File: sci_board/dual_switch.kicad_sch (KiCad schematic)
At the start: 5 parts, among them U8 MIC2009YM6-TR, U9 MIC2009YM6-TR

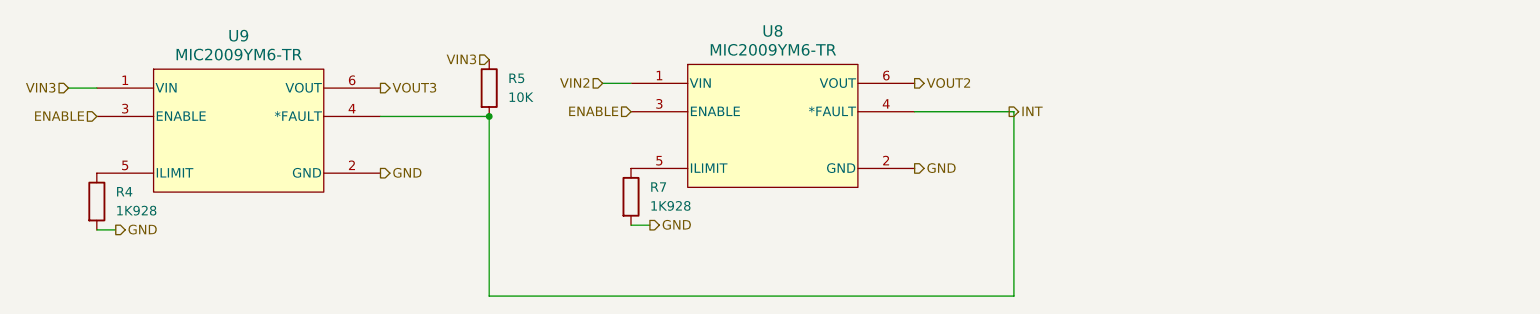
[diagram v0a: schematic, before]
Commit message: SCI board: add flash and mram; decorate PMC with boot, reset, etc
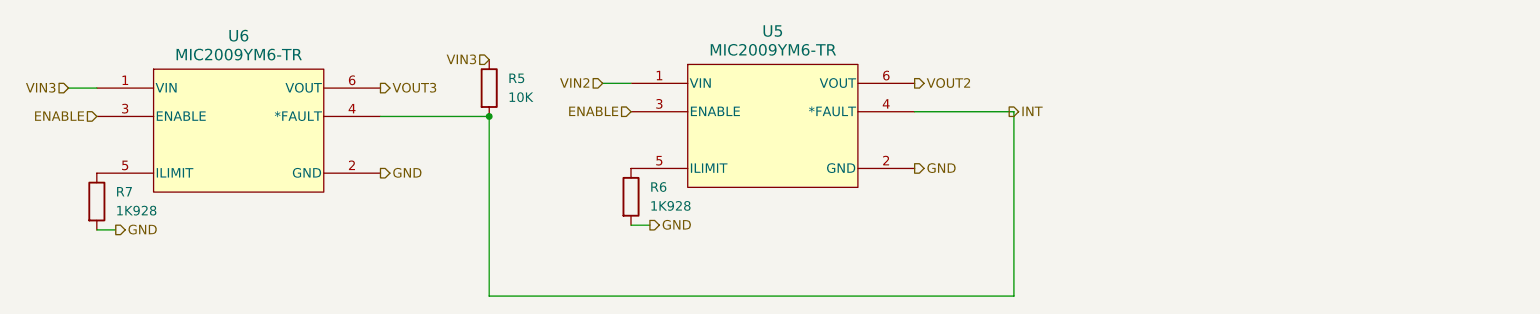
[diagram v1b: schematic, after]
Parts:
- renumbered R7 to R6, R4 to R7, U8 to U5, U9 to U6
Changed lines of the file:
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@@
 		(dnp no)
 		(fields_autoplaced yes)
-		(property "Reference" "U9"
+		(property "Reference" "U6"
 			(at 78.105 61.595 0)
 			(effects
@@
 		(instances
 			(project "sci_board"
-				(path "/b4b2c88d-f6cd-4e60-862d-e21f68728580/14f04065-33ea-4d2f-ac16-5b1240c79b45"
-					(reference "U11")
-					(unit 1)
-				)
-				(path "/b4b2c88d-f6cd-4e60-862d-e21f68728580/599e99f9-ecbe-4b40-92b0-d52ebb90431d"
-					(reference "U9")
-					(unit 1)
-				)
-				(path "/b4b2c88d-f6cd-4e60-862d-e21f68728580/9ec3d894-dc78-4c30-8f58-889c840122ba"
-					(reference "U13")
+				(path "/b4b2c88d-f6cd-4e60-862d-e21f68728580/5e5b27f8-7a4c-45d0-95f8-aff71797fcd3/09c52fbd-a66a-456f-a3b3-a583ddfe7084"
+					(reference "U10")
+					(unit 1)
+				)
+				(path "/b4b2c88d-f6cd-4e60-862d-e21f68728580/5e5b27f8-7a4c-45d0-95f8-aff71797fcd3/270aaf0c-ddf4-417a-965b-076998d870ed"
+					(reference "U8")
+					(unit 1)
+				)
+				(path "/b4b2c88d-f6cd-4e60-862d-e21f68728580/5e5b27f8-7a4c-45d0-95f8-aff71797fcd3/7169f04d-6679-480e-8f54-578d288df681"
+					(reference "U6")
 					(unit 1)
 				)
@@
 		(dnp no)
 		(fields_autoplaced yes)
-		(property "Reference" "U8"
+		(property "Reference" "U5"
 			(at 149.86 60.96 0)
 			(effects
@@
 		(instances
 			(project "sci_board"
-				(path "/b4b2c88d-f6cd-4e60-862d-e21f68728580/14f04065-33ea-4d2f-ac16-5b1240c79b45"
-					(reference "U10")
-					(unit 1)
-				)
-				(path "/b4b2c88d-f6cd-4e60-862d-e21f68728580/599e99f9-ecbe-4b40-92b0-d52ebb90431d"
-					(reference "U8")
-					(unit 1)
-				)
-				(path "/b4b2c88d-f6cd-4e60-862d-e21f68728580/9ec3d894-dc78-4c30-8f58-889c840122ba"
-					(reference "U12")
+				(path "/b4b2c88d-f6cd-4e60-862d-e21f68728580/5e5b27f8-7a4c-45d0-95f8-aff71797fcd3/09c52fbd-a66a-456f-a3b3-a583ddfe7084"
+					(reference "U9")
+					(unit 1)
+				)
+				(path "/b4b2c88d-f6cd-4e60-862d-e21f68728580/5e5b27f8-7a4c-45d0-95f8-aff71797fcd3/270aaf0c-ddf4-417a-965b-076998d870ed"
+					(reference "U7")
+					(unit 1)
+				)
+				(path "/b4b2c88d-f6cd-4e60-862d-e21f68728580/5e5b27f8-7a4c-45d0-95f8-aff71797fcd3/7169f04d-6679-480e-8f54-578d288df681"
+					(reference "U5")
 					(unit 1)
 				)
@@
 		(instances
 			(project "sci_board"
-				(path "/b4b2c88d-f6cd-4e60-862d-e21f68728580/14f04065-33ea-4d2f-ac16-5b1240c79b45"
-					(reference "R6")
-					(unit 1)
-				)
-				(path "/b4b2c88d-f6cd-4e60-862d-e21f68728580/599e99f9-ecbe-4b40-92b0-d52ebb90431d"
+				(path "/b4b2c88d-f6cd-4e60-862d-e21f68728580/5e5b27f8-7a4c-45d0-95f8-aff71797fcd3/09c52fbd-a66a-456f-a3b3-a583ddfe7084"
+					(reference "R11")
+					(unit 1)
+				)
+				(path "/b4b2c88d-f6cd-4e60-862d-e21f68728580/5e5b27f8-7a4c-45d0-95f8-aff71797fcd3/270aaf0c-ddf4-417a-965b-076998d870ed"
+					(reference "R8")
+					(unit 1)
+				)
+				(path "/b4b2c88d-f6cd-4e60-862d-e21f68728580/5e5b27f8-7a4c-45d0-95f8-aff71797fcd3/7169f04d-6679-480e-8f54-578d288df681"
 					(reference "R5")
-					(unit 1)
-				)
-				(path "/b4b2c88d-f6cd-4e60-862d-e21f68728580/9ec3d894-dc78-4c30-8f58-889c840122ba"
-					(reference "R9")
 					(unit 1)
 				)
@@
 		(dnp no)
 		(fields_autoplaced yes)
-		(property "Reference" "R7"
+		(property "Reference" "R6"
 			(at 133.35 81.9149 0)
 			(effects
@@
 		(instances
 			(project "sci_board"
-				(path "/b4b2c88d-f6cd-4e60-862d-e21f68728580/14f04065-33ea-4d2f-ac16-5b1240c79b45"
-					(reference "R7")
-					(unit 1)
-				)
-				(path "/b4b2c88d-f6cd-4e60-862d-e21f68728580/9ec3d894-dc78-4c30-8f58-889c840122ba"
-					(reference "R10")
+				(path "/b4b2c88d-f6cd-4e60-862d-e21f68728580/5e5b27f8-7a4c-45d0-95f8-aff71797fcd3/09c52fbd-a66a-456f-a3b3-a583ddfe7084"
+					(reference "R12")
+					(unit 1)
+				)
+				(path "/b4b2c88d-f6cd-4e60-862d-e21f68728580/5e5b27f8-7a4c-45d0-95f8-aff71797fcd3/270aaf0c-ddf4-417a-965b-076998d870ed"
+					(reference "R9")
+					(unit 1)
+				)
+				(path "/b4b2c88d-f6cd-4e60-862d-e21f68728580/5e5b27f8-7a4c-45d0-95f8-aff71797fcd3/7169f04d-6679-480e-8f54-578d288df681"
+					(reference "R6")
 					(unit 1)
 				)
@@
 		(dnp no)
 		(fields_autoplaced yes)
-		(property "Reference" "R4"
+		(property "Reference" "R7"
 			(at 61.595 82.5499 0)
 			(effects
@@
 		(instances
 			(project "sci_board"
-				(path "/b4b2c88d-f6cd-4e60-862d-e21f68728580/14f04065-33ea-4d2f-ac16-5b1240c79b45"
-					(reference "R8")
-					(unit 1)
-				)
-				(path "/b4b2c88d-f6cd-4e60-862d-e21f68728580/599e99f9-ecbe-4b40-92b0-d52ebb90431d"
-					(reference "R4")
-					(unit 1)
-				)
-				(path "/b4b2c88d-f6cd-4e60-862d-e21f68728580/9ec3d894-dc78-4c30-8f58-889c840122ba"
-					(reference "R11")
-					(unit 1)
-				)
+				(path "/b4b2c88d-f6cd-4e60-862d-e21f68728580/5e5b27f8-7a4c-45d0-95f8-aff71797fcd3/09c52fbd-a66a-456f-a3b3-a583ddfe7084"
+					(reference "R13")
+					(unit 1)
+				)
+				(path "/b4b2c88d-f6cd-4e60-862d-e21f68728580/5e5b27f8-7a4c-45d0-95f8-aff71797fcd3/270aaf0c-ddf4-417a-965b-076998d870ed"
+					(reference "R10")
+					(unit 1)
+				)
+				(path "/b4b2c88d-f6cd-4e60-862d-e21f68728580/5e5b27f8-7a4c-45d0-95f8-aff71797fcd3/7169f04d-6679-480e-8f54-578d288df681"
+					(reference "R7")
+					(unit 1)
+				)

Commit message: start SCI pcb
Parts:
- R11: renamed from R5; footprint (none) -> Resistor_SMD:R_0603_1608Metric_Pad0.98x0.95mm_HandSolder
- R12: renamed from R6; footprint (none) -> Resistor_SMD:R_0603_1608Metric_Pad0.98x0.95mm_HandSolder
- R13: renamed from R7; footprint (none) -> Resistor_SMD:R_0603_1608Metric_Pad0.98x0.95mm_HandSolder
- U10: renamed from U6; footprint Project:SOT-23-6_Handsoldering -> Package_TO_SOT_SMD:SOT-23-6_Handsoldering
- U9: renamed from U5; footprint Project:SOT-23-6_Handsoldering -> Package_TO_SOT_SMD:SOT-23-6_Handsoldering
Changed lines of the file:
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@@
 		(dnp no)
 		(fields_autoplaced yes)
-		(property "Reference" "U6"
+		(property "Reference" "U10"
 			(at 78.105 61.595 0)
 			(effects
@@
 			)
 		)
-		(property "Footprint" "Project:SOT-23-6_Handsoldering"
+		(property "Footprint" "Package_TO_SOT_SMD:SOT-23-6_Handsoldering"
 			(at 70.993 64.008 0)
 			(effects
@@
 		(dnp no)
 		(fields_autoplaced yes)
-		(property "Reference" "U5"
+		(property "Reference" "U9"
 			(at 149.86 60.96 0)
 			(effects
@@
 			)
 		)
-		(property "Footprint" "Project:SOT-23-6_Handsoldering"
+		(property "Footprint" "Package_TO_SOT_SMD:SOT-23-6_Handsoldering"
 			(at 142.748 63.373 0)
 			(effects
@@
 		(dnp no)
 		(fields_autoplaced yes)
-		(property "Reference" "R5"
+		(property "Reference" "R11"
 			(at 114.3 67.3099 0)
 			(effects
@@
 			)
 		)
-		(property "Footprint" ""
+		(property "Footprint" "Resistor_SMD:R_0603_1608Metric_Pad0.98x0.95mm_HandSolder"
 			(at 109.982 68.58 90)
 			(effects
@@
 		(dnp no)
 		(fields_autoplaced yes)
-		(property "Reference" "R6"
+		(property "Reference" "R12"
 			(at 133.35 81.9149 0)
 			(effects
@@
 			)
 		)
-		(property "Footprint" ""
+		(property "Footprint" "Resistor_SMD:R_0603_1608Metric_Pad0.98x0.95mm_HandSolder"
 			(at 129.032 83.185 90)
 			(effects
@@
 		(dnp no)
 		(fields_autoplaced yes)
-		(property "Reference" "R7"
+		(property "Reference" "R13"
 			(at 61.595 82.5499 0)
 			(effects
@@
 			)
 		)
-		(property "Footprint" ""
+		(property "Footprint" "Resistor_SMD:R_0603_1608Metric_Pad0.98x0.95mm_HandSolder"
 			(at 57.277 83.82 90)
 			(effects

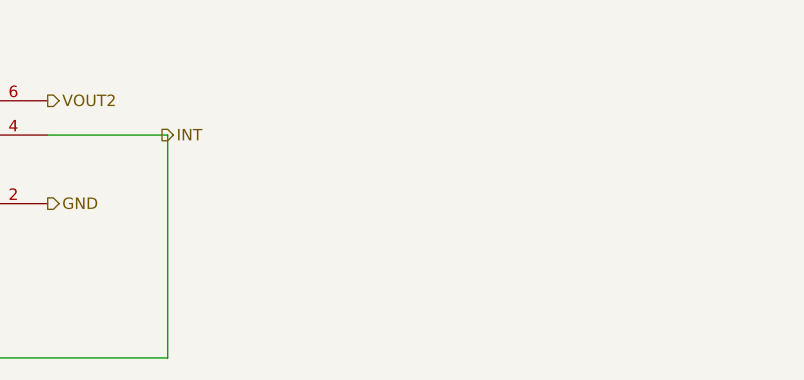
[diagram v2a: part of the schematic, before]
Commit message: cameras have fcp connectors, use data 2:9, and need a clock
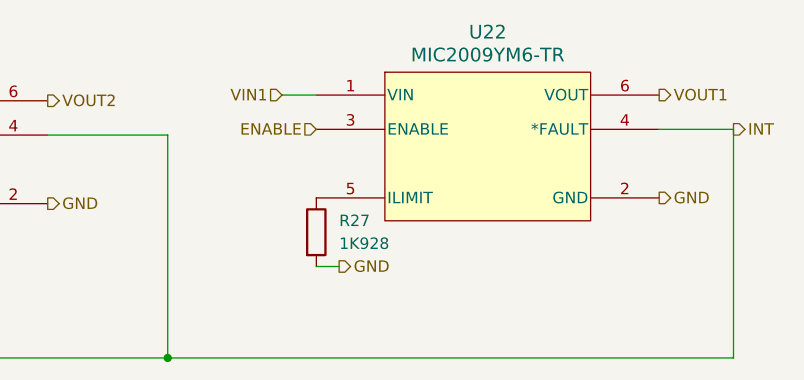
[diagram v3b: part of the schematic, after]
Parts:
- added R27: 1K928, Resistor_SMD:R_0603_1608Metric_Pad0.98x0.95mm_HandSolder, symbol Device:R
- added U22: MIC2009YM6-TR, Package_TO_SOT_SMD:SOT-23-6_Handsoldering, symbol Project:MIC2009YM6-TR
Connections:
- net ENABLE: now also U22.3 (ENABLE)
- net GND: now also R27.2, U22.2 (GND)
- net INT: now also U22.4 (*FAULT)
- new net: R27.1, U22.5 (ILIMIT)
- new net VIN1: U22.1 (VIN)
- new net VOUT1: U22.6 (VOUT)

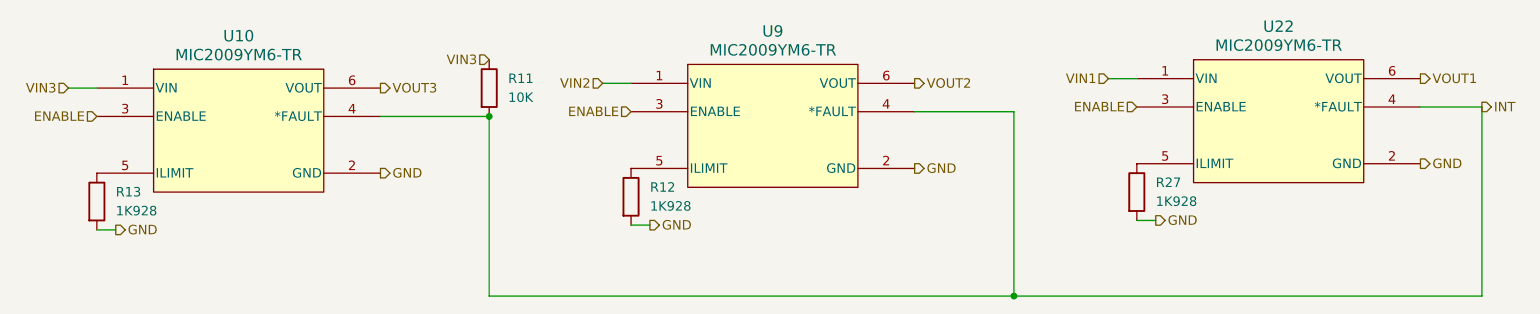
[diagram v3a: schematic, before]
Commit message: begin to update the pcb
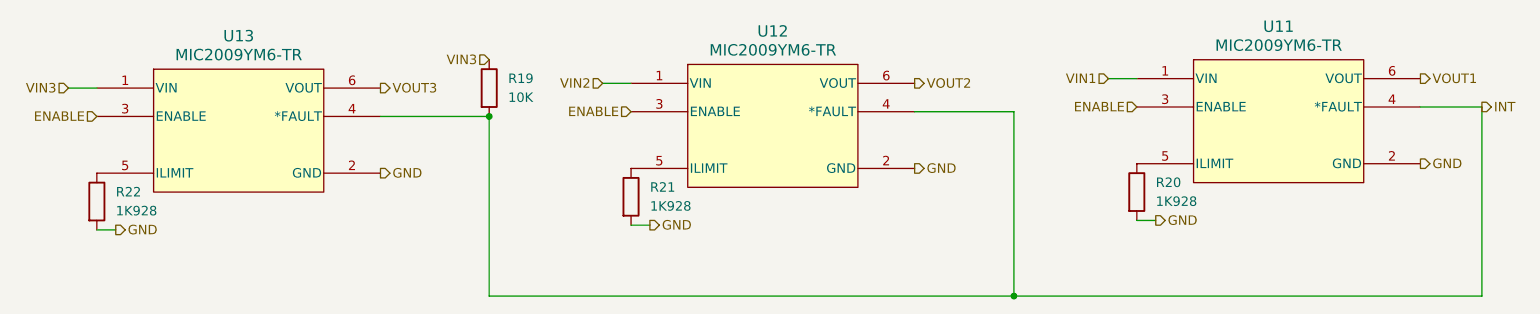
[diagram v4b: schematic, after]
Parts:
- renumbered R11 to R19, R27 to R20, R12 to R21, R13 to R22, U22 to U11, U9 to U12, U10 to U13
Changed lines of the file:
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@@
 		(dnp no)
 		(fields_autoplaced yes)
-		(property "Reference" "U10"
+		(property "Reference" "U13"
 			(at 78.105 61.595 0)
 			(effects
@@
 			(project "sci_board"
 				(path "/b4b2c88d-f6cd-4e60-862d-e21f68728580/5e5b27f8-7a4c-45d0-95f8-aff71797fcd3/09c52fbd-a66a-456f-a3b3-a583ddfe7084"
+					(reference "U13")
+					(unit 1)
+				)
+				(path "/b4b2c88d-f6cd-4e60-862d-e21f68728580/5e5b27f8-7a4c-45d0-95f8-aff71797fcd3/3113fc14-4b9f-4852-8ddb-4c564d791d7f"
+					(reference "U7")
+					(unit 1)
+				)
+				(path "/b4b2c88d-f6cd-4e60-862d-e21f68728580/5e5b27f8-7a4c-45d0-95f8-aff71797fcd3/df99859d-8e37-4f21-a1c5-637d9e74b907"
 					(reference "U10")
-					(unit 1)
-				)
-				(path "/b4b2c88d-f6cd-4e60-862d-e21f68728580/5e5b27f8-7a4c-45d0-95f8-aff71797fcd3/3113fc14-4b9f-4852-8ddb-4c564d791d7f"
-					(reference "U7")
-					(unit 1)
-				)
-				(path "/b4b2c88d-f6cd-4e60-862d-e21f68728580/5e5b27f8-7a4c-45d0-95f8-aff71797fcd3/df99859d-8e37-4f21-a1c5-637d9e74b907"
-					(reference "U21")
 					(unit 1)
 				)
@@
 		(dnp no)
 		(fields_autoplaced yes)
-		(property "Reference" "R27"
+		(property "Reference" "R20"
 			(at 201.295 81.2799 0)
 			(effects
@@
 			(project "sci_board"
 				(path "/b4b2c88d-f6cd-4e60-862d-e21f68728580/5e5b27f8-7a4c-45d0-95f8-aff71797fcd3/09c52fbd-a66a-456f-a3b3-a583ddfe7084"
-					(reference "R27")
-					(unit 1)
-				)
-				(path "/b4b2c88d-f6cd-4e60-862d-e21f68728580/5e5b27f8-7a4c-45d0-95f8-aff71797fcd3/3113fc14-4b9f-4852-8ddb-4c564d791d7f"
-					(reference "R6")
-					(unit 1)
-				)
-				(path "/b4b2c88d-f6cd-4e60-862d-e21f68728580/5e5b27f8-7a4c-45d0-95f8-aff71797fcd3/df99859d-8e37-4f21-a1c5-637d9e74b907"
-					(reference "R10")
+					(reference "R20")
+					(unit 1)
+				)
+				(path "/b4b2c88d-f6cd-4e60-862d-e21f68728580/5e5b27f8-7a4c-45d0-95f8-aff71797fcd3/3113fc14-4b9f-4852-8ddb-4c564d791d7f"
+					(reference "R12")
+					(unit 1)
+				)
+				(path "/b4b2c88d-f6cd-4e60-862d-e21f68728580/5e5b27f8-7a4c-45d0-95f8-aff71797fcd3/df99859d-8e37-4f21-a1c5-637d9e74b907"
+					(reference "R16")
 					(unit 1)
 				)
@@
 		(dnp no)
 		(fields_autoplaced yes)
-		(property "Reference" "U9"
+		(property "Reference" "U12"
 			(at 149.86 60.96 0)
 			(effects
@@
 			(project "sci_board"
 				(path "/b4b2c88d-f6cd-4e60-862d-e21f68728580/5e5b27f8-7a4c-45d0-95f8-aff71797fcd3/09c52fbd-a66a-456f-a3b3-a583ddfe7084"
+					(reference "U12")
+					(unit 1)
+				)
+				(path "/b4b2c88d-f6cd-4e60-862d-e21f68728580/5e5b27f8-7a4c-45d0-95f8-aff71797fcd3/3113fc14-4b9f-4852-8ddb-4c564d791d7f"
+					(reference "U6")
+					(unit 1)
+				)
+				(path "/b4b2c88d-f6cd-4e60-862d-e21f68728580/5e5b27f8-7a4c-45d0-95f8-aff71797fcd3/df99859d-8e37-4f21-a1c5-637d9e74b907"
 					(reference "U9")
-					(unit 1)
-				)
-				(path "/b4b2c88d-f6cd-4e60-862d-e21f68728580/5e5b27f8-7a4c-45d0-95f8-aff71797fcd3/3113fc14-4b9f-4852-8ddb-4c564d791d7f"
-					(reference "U6")
-					(unit 1)
-				)
-				(path "/b4b2c88d-f6cd-4e60-862d-e21f68728580/5e5b27f8-7a4c-45d0-95f8-aff71797fcd3/df99859d-8e37-4f21-a1c5-637d9e74b907"
-					(reference "U20")
 					(unit 1)
 				)
@@
 		(dnp no)
 		(fields_autoplaced yes)
-		(property "Reference" "R11"
+		(property "Reference" "R19"
 			(at 114.3 67.3099 0)
 			(effects
@@
 			(project "sci_board"
 				(path "/b4b2c88d-f6cd-4e60-862d-e21f68728580/5e5b27f8-7a4c-45d0-95f8-aff71797fcd3/09c52fbd-a66a-456f-a3b3-a583ddfe7084"
+					(reference "R19")
+					(unit 1)
+				)
+				(path "/b4b2c88d-f6cd-4e60-862d-e21f68728580/5e5b27f8-7a4c-45d0-95f8-aff71797fcd3/3113fc14-4b9f-4852-8ddb-4c564d791d7f"
 					(reference "R11")
 					(unit 1)
 				)
-				(path "/b4b2c88d-f6cd-4e60-862d-e21f68728580/5e5b27f8-7a4c-45d0-95f8-aff71797fcd3/3113fc14-4b9f-4852-8ddb-4c564d791d7f"
-					(reference "R5")
-					(unit 1)
-				)
-				(path "/b4b2c88d-f6cd-4e60-862d-e21f68728580/5e5b27f8-7a4c-45d0-95f8-aff71797fcd3/df99859d-8e37-4f21-a1c5-637d9e74b907"
-					(reference "R9")
+				(path "/b4b2c88d-f6cd-4e60-862d-e21f68728580/5e5b27f8-7a4c-45d0-95f8-aff71797fcd3/df99859d-8e37-4f21-a1c5-637d9e74b907"
+					(reference "R15")
 					(unit 1)
 				)
@@
 		(dnp no)
 		(fields_autoplaced yes)
-		(property "Reference" "U22"
+		(property "Reference" "U11"
 			(at 217.805 60.325 0)
 			(effects
@@
 			(project "sci_board"
 				(path "/b4b2c88d-f6cd-4e60-862d-e21f68728580/5e5b27f8-7a4c-45d0-95f8-aff71797fcd3/09c52fbd-a66a-456f-a3b3-a583ddfe7084"
-					(reference "U22")
+					(reference "U11")
 					(unit 1)
 				)
@@
 		(dnp no)
 		(fields_autoplaced yes)
-		(property "Reference" "R12"
+		(property "Reference" "R21"
 			(at 133.35 81.9149 0)
 			(effects
@@
 			(project "sci_board"
 				(path "/b4b2c88d-f6cd-4e60-862d-e21f68728580/5e5b27f8-7a4c-45d0-95f8-aff71797fcd3/09c52fbd-a66a-456f-a3b3-a583ddfe7084"
-					(reference "R12")
-					(unit 1)
-				)
-				(path "/b4b2c88d-f6cd-4e60-862d-e21f68728580/5e5b27f8-7a4c-45d0-95f8-aff71797fcd3/3113fc14-4b9f-4852-8ddb-4c564d791d7f"
-					(reference "R7")
-					(unit 1)
-				)
-				(path "/b4b2c88d-f6cd-4e60-862d-e21f68728580/5e5b27f8-7a4c-45d0-95f8-aff71797fcd3/df99859d-8e37-4f21-a1c5-637d9e74b907"
-					(reference "R25")
+					(reference "R21")
+					(unit 1)
+				)
+				(path "/b4b2c88d-f6cd-4e60-862d-e21f68728580/5e5b27f8-7a4c-45d0-95f8-aff71797fcd3/3113fc14-4b9f-4852-8ddb-4c564d791d7f"
+					(reference "R13")
+					(unit 1)
+				)
+				(path "/b4b2c88d-f6cd-4e60-862d-e21f68728580/5e5b27f8-7a4c-45d0-95f8-aff71797fcd3/df99859d-8e37-4f21-a1c5-637d9e74b907"
+					(reference "R17")
 					(unit 1)
 				)
@@
 		(dnp no)
 		(fields_autoplaced yes)
-		(property "Reference" "R13"
+		(property "Reference" "R22"
 			(at 61.595 82.5499 0)
 			(effects
@@
 			(project "sci_board"
 				(path "/b4b2c88d-f6cd-4e60-862d-e21f68728580/5e5b27f8-7a4c-45d0-95f8-aff71797fcd3/09c52fbd-a66a-456f-a3b3-a583ddfe7084"
-					(reference "R13")
-					(unit 1)
-				)
-				(path "/b4b2c88d-f6cd-4e60-862d-e21f68728580/5e5b27f8-7a4c-45d0-95f8-aff71797fcd3/3113fc14-4b9f-4852-8ddb-4c564d791d7f"
-					(reference "R8")
-					(unit 1)
-				)
-				(path "/b4b2c88d-f6cd-4e60-862d-e21f68728580/5e5b27f8-7a4c-45d0-95f8-aff71797fcd3/df99859d-8e37-4f21-a1c5-637d9e74b907"
-					(reference "R26")
-					(unit 1)
-				)
+					(reference "R22")
+					(unit 1)
+				)
+				(path "/b4b2c88d-f6cd-4e60-862d-e21f68728580/5e5b27f8-7a4c-45d0-95f8-aff71797fcd3/3113fc14-4b9f-4852-8ddb-4c564d791d7f"
+					(reference "R14")
+					(unit 1)
+				)
+				(path "/b4b2c88d-f6cd-4e60-862d-e21f68728580/5e5b27f8-7a4c-45d0-95f8-aff71797fcd3/df99859d-8e37-4f21-a1c5-637d9e74b907"
+					(reference "R18")
+					(unit 1)
+				)
